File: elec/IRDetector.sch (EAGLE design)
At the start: 22 parts, among them IC1 TL082P, IC2 TL082P, IC3 TL082P, T1 QSD124N

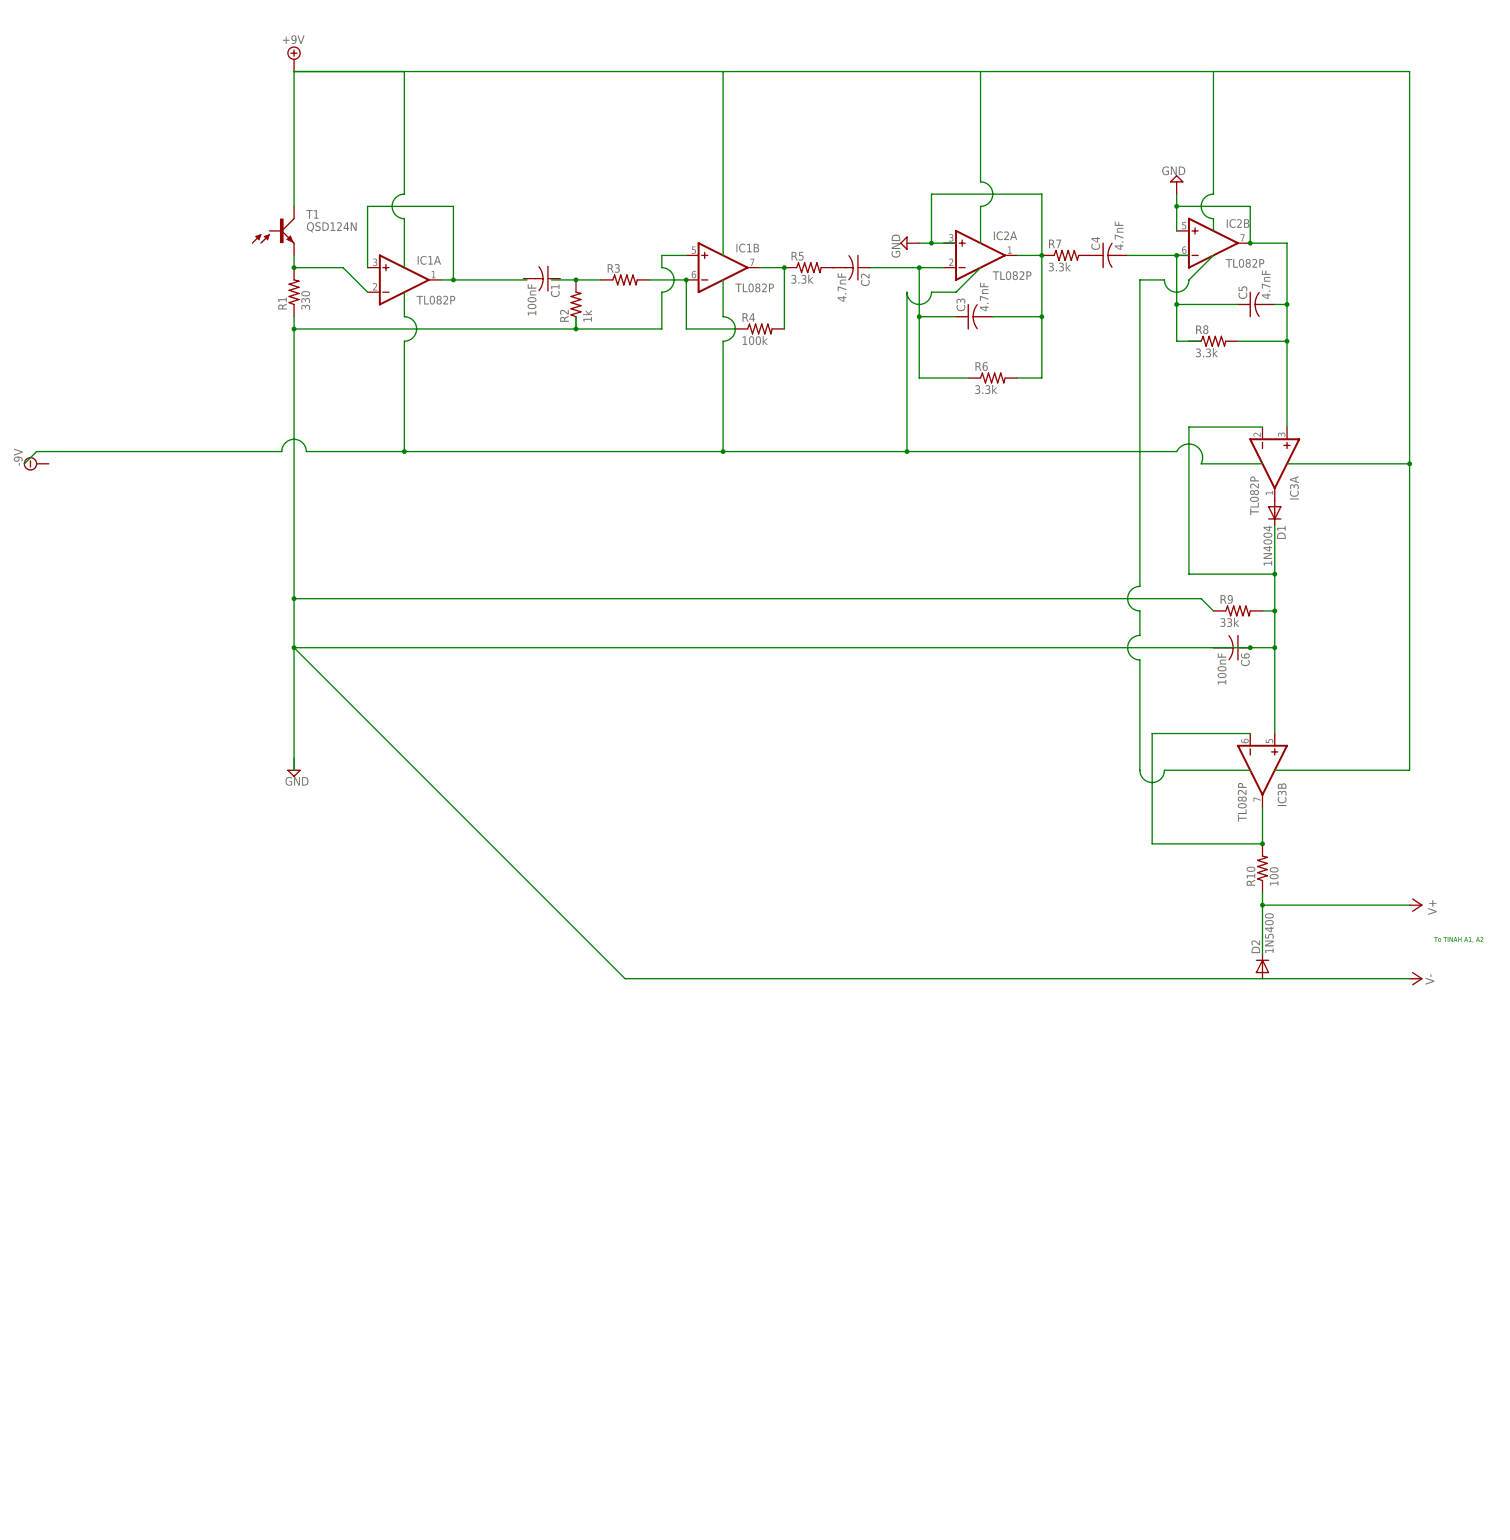
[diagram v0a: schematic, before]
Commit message: Circuit pictures for website added
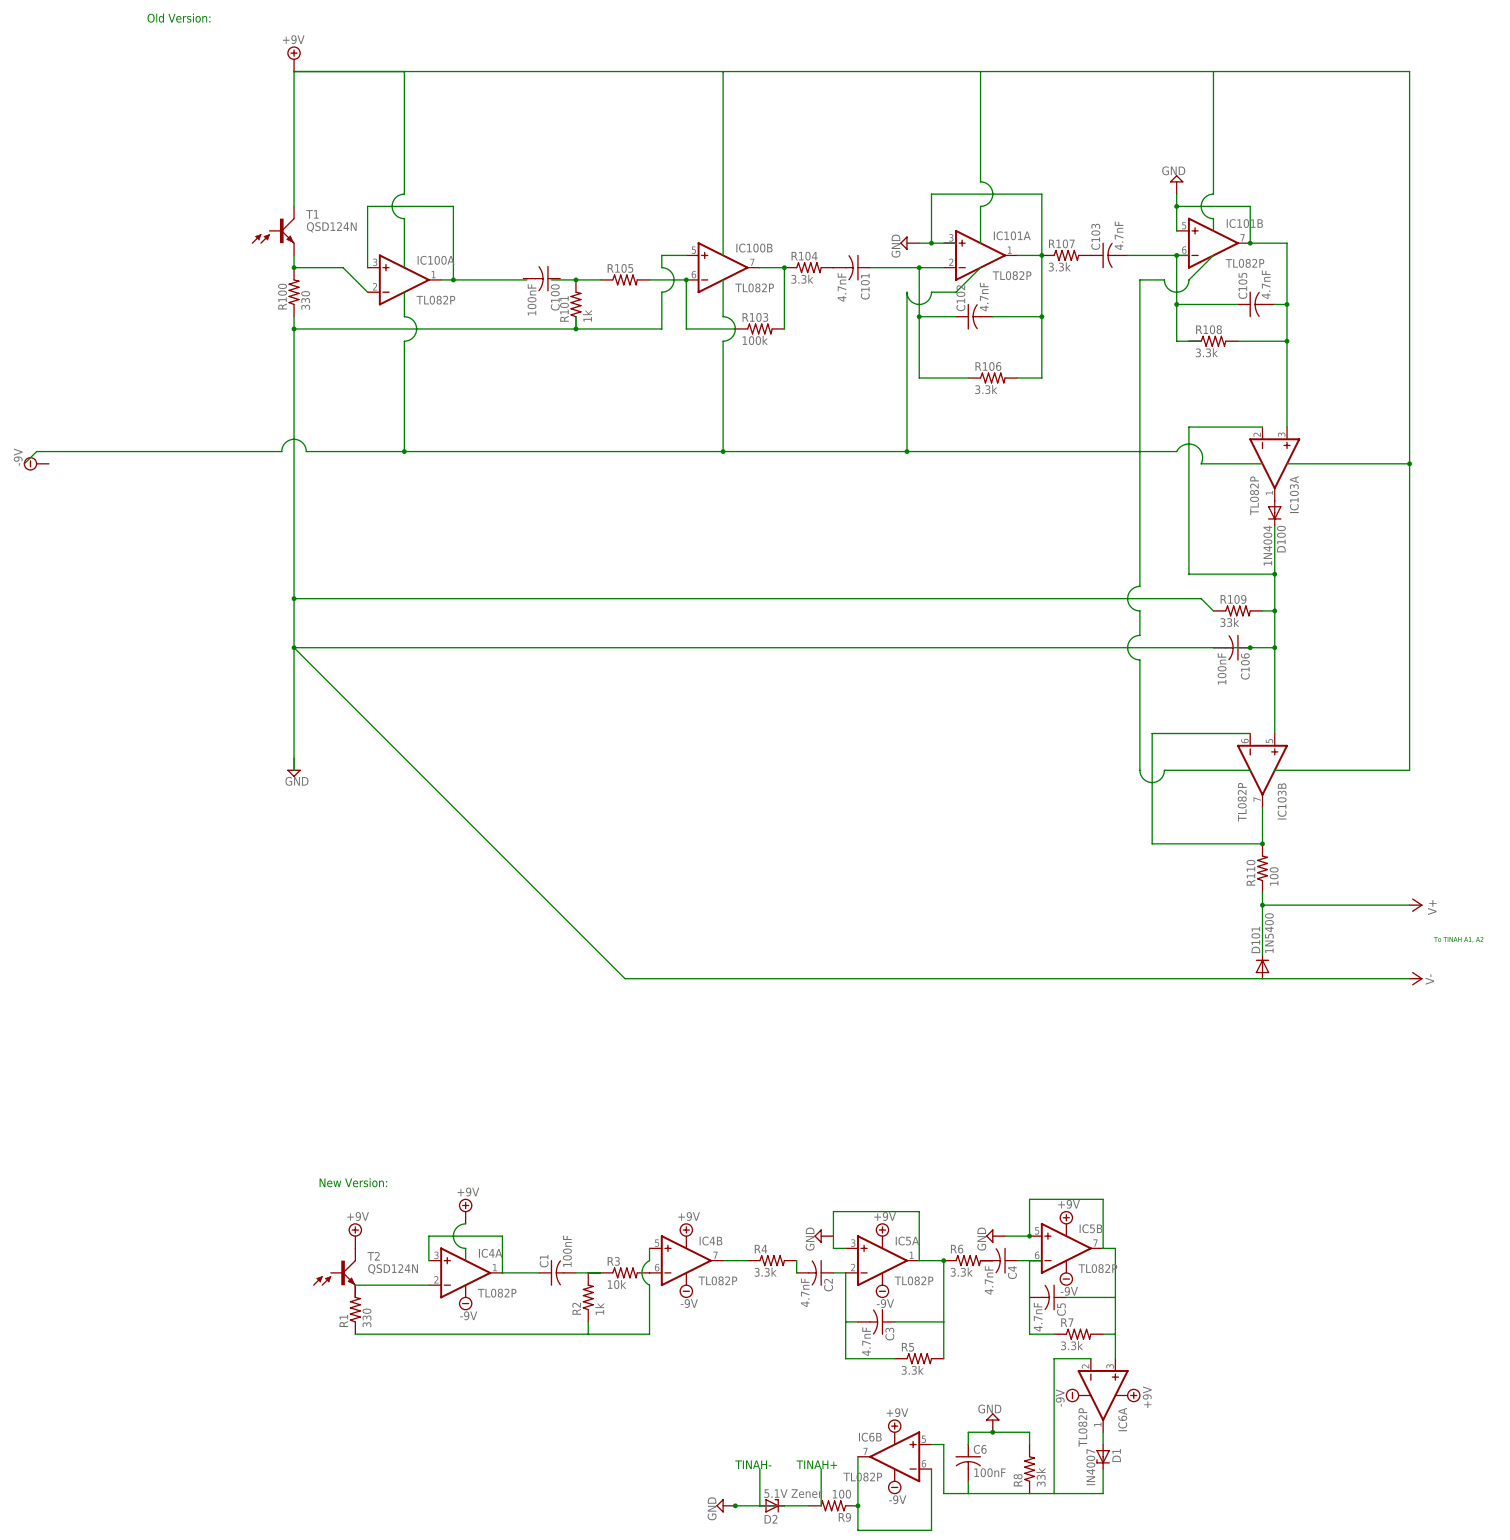
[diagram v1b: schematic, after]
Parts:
- added C100: 100nF, resistor:C-US025-024X044
- added C101: 4.7nF, resistor:C-US025-025X050
- added C102: 4.7nF, resistor:C-US050-055X075
- added C103: 4.7nF, resistor:C-US225-087X268
- added C105: 4.7nF, resistor:C-US050-045X075
- added C106: 100nF, resistor:C-US025-060X050
- added D100: 1N4004, diode:1N4004
- added D101: 1N5400, diode:1N5400
- added IC4, IC5, IC6: TL082P, linear:TL082P
- added R100: 330, resistor:R-US_0204/5
- added R101: 1k, resistor:R-US_0204/5
- added R103: 100k, resistor:R-US_01005
- added R104: 3.3k, resistor:R-US_01005
- added R105: (no value), resistor:R-US_0207/5V
- added R106, R107: 3.3k, resistor:R-US_0207/5V
- added R108: 3.3k, resistor:R-US_0309/12
- added R109: 33k, resistor:R-US_0207/5V
- added T2: QSD124N, opto-trans-siemens:BP103
- C3: device resistor:C-US050-055X075 -> resistor:C-US025-025X050
- C4: device resistor:C-US225-087X268 -> resistor:C-US025-025X050
- C5: device resistor:C-US050-045X075 -> resistor:C-US025-025X050
- D1: value 1N4004 -> IN4007; device diode:1N4004 -> diode:ZENER-DIODEZD-5
- D2: value 1N5400 -> 5.1V Zener; device diode:1N5400 -> diode:ZENER-DIODEZD-5
- R3: value (none) -> 10k; device resistor:R-US_0207/5V -> resistor:R-US_0204/2V
- R4: value 100k -> 3.3k
- R5: device resistor:R-US_01005 -> resistor:R-US_0207/5V
- R6: device resistor:R-US_0207/5V -> resistor:R-US_01005
- R8: value 3.3k -> 33k; device resistor:R-US_0309/12 -> resistor:R-US_0207/5V
- R9: value 33k -> 100; device resistor:R-US_0207/5V -> resistor:R-US_0414/5V
- renumbered IC1 to IC100, IC2 to IC101, IC3 to IC103, R10 to R110
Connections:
- new net +9V: T2.C
- new net N$10: IC4A.-IN, R1.2
- new net N$11: C1.1, IC4A.+IN, IC4A.OUT
- new net N$16: IC4B.OUT, R4.1
- new net N$17: C1.2, R2.2, R3.1
- new net N$18: IC4B.-IN, R3.2
- new net N$19: IC4B.+IN, R1.1, R2.1
- new net N$20: C2.1, C3.2, IC5A.-IN, R5.1
- new net N$21: C2.2, R4.2
- new net N$22: C4.1, C5.2, R7.1
- new net N$23: D1.A, IC6A.OUT
- new net N$24: C6.2, D1.C, IC6A.-IN, IC6B.+IN, R8.1
- new net N$25: IC6B.-IN, IC6B.OUT, R9.1
- net GND: now also C102.2, C105.2, C3.1, C5.1, C6.1, D2.A, D2.C, IC5A.+IN, IC5A.OUT, IC5B.+IN, IC5B.OUT, IC6A.+IN, R106.2, R107.1, R108.2, R5.2, R6.1, R7.2, R9.2; no longer C3.2, C5.2, R6.2, R7.1
- net N$1: now also R100.2; no longer R1.2
- net N$13: now also C103.1, R107.2; no longer C4.1, R7.2
- net N$14: now also C103.2, C105.1, R108.1; no longer C4.2, C5.1, R8.1
- net N$4: now also R103.1, R105.2; no longer R3.2, R4.1
- net N$5: now also R103.2, R104.1; no longer R4.2, R5.1
- net N$6: now also R101.2, R105.1; no longer R2.2, R3.1
- net N$7: now also C101.1, C102.1, R106.1; no longer C2.1, C3.1, R6.1
- net N$8: now also C101.2, R104.2; no longer C2.2, R5.2
- net N$9: now also D100.A; no longer D1.A
- net V+: now also D101.C; no longer D2.C
- net V-: now also C106.1, C106.2, D100.C, D101.A, R100.1, R101.1, R109.1, R109.2; no longer C6.1, C6.2, D1.C, D2.A, R1.1, R2.1, R9.1, R9.2
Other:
- note added: "New Version:"
- note added: "Old Version:"
- note added: "TINAH+"
- note added: "TINAH-"
- moved on the sheet: C1, C2, C3, C4, C5, C6, R1, R2, R3, R4, R5, R6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
